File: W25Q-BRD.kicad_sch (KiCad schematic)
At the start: 7 parts, among them J1 QSPI, U1 W25Q128JVSIQ

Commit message: Version 1.1. Added 2 caps. Added few texts.
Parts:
- added C1: 100nF, Capacitor_SMD:C_0402_1005Metric, symbol Device:C_Small
- added C2: 1uF, Capacitor_SMD:C_0603_1608Metric, symbol Device:C_Small
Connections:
- net +3.3V: now also C1.1, C2.1
- net GND: now also C1.2, C2.2
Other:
- title: W25Q-BRD-0010 -> W25Q-BRD-0011
- moved on the sheet: U1

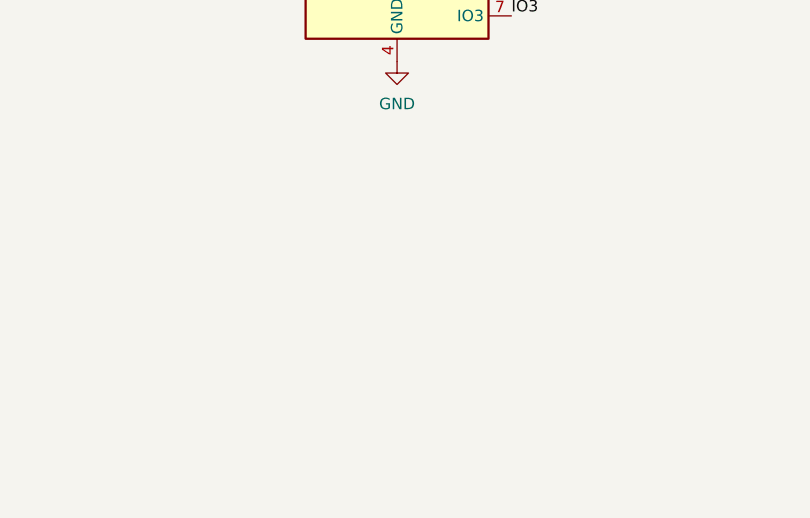
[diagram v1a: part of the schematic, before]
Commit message: Added alternative footprint for WSOT-8 version of the chip.
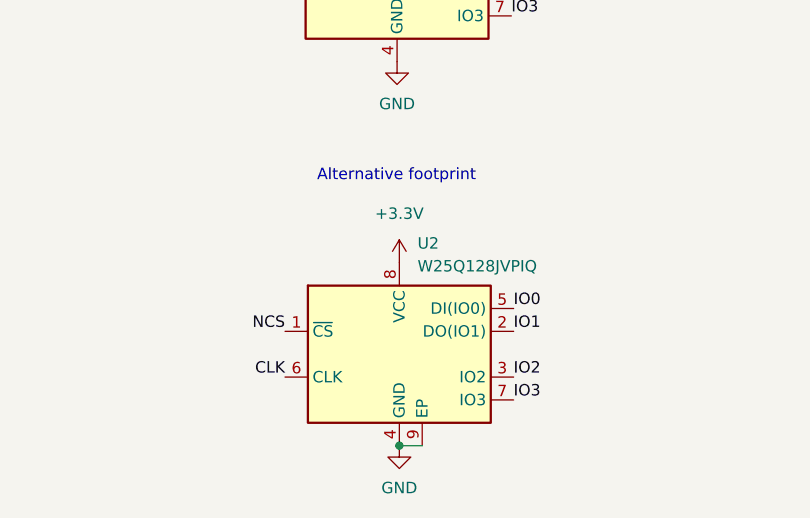
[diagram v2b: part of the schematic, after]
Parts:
- added U2: W25Q128JVPIQ, Package_SON:WSON-8-1EP_6x5mm_P1.27mm_EP3.4x4.3mm, symbol Memory_Flash:W25Q32JVZP
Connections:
- net +3.3V: now also U2.8 (VCC)
- net CLK: now also U2.6 (CLK)
- net GND: now also U2.4 (GND), U2.9 (EP)
- net IO0: now also U2.5 (DI(IO0))
- net IO1: now also U2.2 (DO(IO1))
- net IO2: now also U2.3 (IO2)
- net IO3: now also U2.7 (IO3)
- net NCS: now also U2.1 (~{CS})
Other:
- note added: "Alternative footprint"
- title: W25Q-BRD-0011 -> W25Q-BRD-0012
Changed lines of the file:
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@@
   (paper "A4")
   (title_block
-    (title "W25Q-BRD-0011")
+    (title "W25Q-BRD-0012")
     (date "2022-12-05")
-    (rev "1.1")
+    (rev "1.2")
     (company "(c) Andriy Golovnya")
     (comment 1 "Breakout board for W25Q QSPI flash chips family")
   )
+  (junction (at 165.227 140.589) (diameter 0) (color 0 0 0 0)
+  )
+  (wire (pts (xy 165.227 140.589) (xy 167.767 140.589))
+    (stroke (width 0) (type default) (color 0 0 0 0))
+  )
+  (text "Alternative footprint" (at 156.083 111.379 0)
+    (effects (font (size 1.27 1.27)) (justify left bottom))
+  )
   (label "IO2" (at 177.673 90.297 0)
     (effects (font (size 1.27 1.27)) (justify left bottom))
   )
+  (label "CLK" (at 152.527 132.969 180)
+    (effects (font (size 1.27 1.27)) (justify right bottom))
+  )
   (label "IO2" (at 218.186 88.519 180)
     (effects (font (size 1.27 1.27)) (justify right bottom))
   )
+  (label "IO1" (at 177.927 127.889 0)
+    (effects (font (size 1.27 1.27)) (justify left bottom))
+  )
   (label "IO0" (at 218.186 83.439 180)
     (effects (font (size 1.27 1.27)) (justify right bottom))
@@
     (effects (font (size 1.27 1.27)) (justify right bottom))
   )
+  (label "IO3" (at 177.927 135.509 0)
+    (effects (font (size 1.27 1.27)) (justify left bottom))
+  )
+  (label "NCS" (at 152.527 127.889 180)
+    (effects (font (size 1.27 1.27)) (justify right bottom))
+  )
   (label "IO1" (at 177.673 85.217 0)
     (effects (font (size 1.27 1.27)) (justify left bottom))
@@
     (effects (font (size 1.27 1.27)) (justify right bottom))
   )
+  (label "IO2" (at 177.927 132.969 0)
+    (effects (font (size 1.27 1.27)) (justify left bottom))
+  )
   (label "IO3" (at 218.186 91.059 180)
     (effects (font (size 1.27 1.27)) (justify right bottom))
@@
   (label "NCS" (at 76.327 93.98 270)
     (effects (font (size 1.27 1.27)) (justify right bottom))
+  )
+  (label "IO0" (at 177.927 125.349 0)
+    (effects (font (size 1.27 1.27)) (justify left bottom))
   )
   (symbol (lib_id "Device:LED") (at 76.327 85.09 90) (unit 1)
@@
   (symbol (lib_id "power:GND") (at 234.442 88.011 0) (unit 1)
     (in_bom yes) (on_board yes) (fields_autoplaced)
-    (property "Reference" "#PWR012" (id 0) (at 234.442 94.361 0)
+    (property "Reference" "#PWR014" (id 0) (at 234.442 94.361 0)
       (effects (font (size 1.27 1.27)) hide)
     )
@@
     )
     (property "Datasheet" "" (id 3) (at 234.442 88.011 0)
+      (effects (font (size 1.27 1.27)) hide)
+    )
+    (pin "1")
+  )
+  (symbol (lib_id "power:GND") (at 165.227 140.589 0) (unit 1)
+    (in_bom yes) (on_board yes) (fields_autoplaced)
+    (property "Reference" "#PWR011" (id 0) (at 165.227 146.939 0)
+      (effects (font (size 1.27 1.27)) hide)
+    )
+    (property "Value" "GND" (id 1) (at 165.227 145.288 0))
+    (property "Footprint" "" (id 2) (at 165.227 140.589 0)
+      (effects (font (size 1.27 1.27)) hide)
+    )
+    (property "Datasheet" "" (id 3) (at 165.227 140.589 0)
       (effects (font (size 1.27 1.27)) hide)
     )
@@
   (symbol (lib_id "power:+3.3V") (at 218.186 78.359 0) (unit 1)
     (in_bom yes) (on_board yes) (fields_autoplaced)
-    (property "Reference" "#PWR010" (id 0) (at 218.186 82.169 0)
+    (property "Reference" "#PWR012" (id 0) (at 218.186 82.169 0)
       (effects (font (size 1.27 1.27)) hide)
     )
@@
     (pin "1")
   )
+  (symbol (lib_id "Memory_Flash:W25Q32JVZP") (at 165.227 130.429 0) (unit 1)
+    (in_bom yes) (on_board yes) (fields_autoplaced)
+    (property "Reference" "U2" (id 0) (at 167.2464 118.11 0)
+      (effects (font (size 1.27 1.27)) (justify left))
+    )
+    (property "Value" "W25Q128JVPIQ" (id 1) (at 167.2464 120.65 0)
+      (effects (font (size 1.27 1.27)) (justify left))
+    )
+    (property "Footprint" "Package_SON:WSON-8-1EP_6x5mm_P1.27mm_EP3.4x4.3mm" (id 2) (at 165.227 130.429 0)
+      (effects (font (size 1.27 1.27)) hide)
+    )
+    (property "Datasheet" "http://www.winbond.com/resource-files/w25q32jv%20revg%2003272018%20plus.pdf" (id 3) (at 165.227 130.429 0)
+      (effects (font (size 1.27 1.27)) hide)
+    )
+    (pin "1")
+    (pin "2")
+    (pin "3")
+    (pin "4")
+    (pin "5")
+    (pin "6")
+    (pin "7")
+    (pin "8")
+    (pin "9")
+  )
+  (symbol (lib_id "power:+3.3V") (at 165.227 120.269 0) (unit 1)
+    (in_bom yes) (on_board yes) (fields_autoplaced)
+    (property "Reference" "#PWR010" (id 0) (at 165.227 124.079 0)
+      (effects (font (size 1.27 1.27)) hide)
+    )
+    (property "Value" "+3.3V" (id 1) (at 165.227 114.808 0))
+    (property "Footprint" "" (id 2) (at 165.227 120.269 0)
+      (effects (font (size 1.27 1.27)) hide)
+    )
+    (property "Datasheet" "" (id 3) (at 165.227 120.269 0)
+      (effects (font (size 1.27 1.27)) hide)
+    )
+    (pin "1")
+  )
   (symbol (lib_id "power:GND") (at 63.5 93.726 0) (unit 1)
     (in_bom yes) (on_board yes) (fields_autoplaced)
@@
   (symbol (lib_id "power:GND") (at 218.186 96.139 0) (unit 1)
     (in_bom yes) (on_board yes) (fields_autoplaced)
-    (property "Reference" "#PWR011" (id 0) (at 218.186 102.489 0)
+    (property "Reference" "#PWR013" (id 0) (at 218.186 102.489 0)
       (effects (font (size 1.27 1.27)) hide)
     )
@@
       (reference "#PWR09") (unit 1) (value "GND") (footprint "")
     )
+    (path "/f6a8ed41-71d0-4579-ac65-f09060d4f2ae"
+      (reference "#PWR010") (unit 1) (value "+3.3V") (footprint "")
+    )
+    (path "/2ba2bfdb-c495-4ab4-8899-63de27b339a8"
+      (reference "#PWR011") (unit 1) (value "GND") (footprint "")
+    )
     (path "/ee24dd49-6aa5-47f0-acca-d22411addcba"
-      (reference "#PWR010") (unit 1) (value "+3.3V") (footprint "")
+      (reference "#PWR012") (unit 1) (value "+3.3V") (footprint "")
     )
     (path "/fd4c280f-201c-4185-b6cb-e0fa708fbfa6"
-      (reference "#PWR011") (unit 1) (value "GND") (footprint "")
+      (reference "#PWR013") (unit 1) (value "GND") (footprint "")
     )
     (path "/2b3aa814-4ead-4442-9a2f-2dd598e71cb4"
-      (reference "#PWR012") (unit 1) (value "GND") (footprint "")
+      (reference "#PWR014") (unit 1) (value "GND") (footprint "")
     )
     (path "/6b170730-4fc0-49d2-9bc2-738d078e761c"
@@
       (reference "U1") (unit 1) (value "W25Q128JVSIQ") (footprint "Package_SO:SOIC-8_5.23x5.23mm_P1.27mm")
     )
-  )
+    (path "/efff6f51-96f7-42cc-9d7c-85b159b11f9a"
+      (reference "U2") (unit 1) (value "W25Q128JVPIQ") (footprint "Package_SON:WSON-8-1EP_6x5mm_P1.27mm_EP3.4x4.3mm")
+    )
+  )
